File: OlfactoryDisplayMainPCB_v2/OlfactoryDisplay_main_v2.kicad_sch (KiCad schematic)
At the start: 20 parts, among them J1 B2B-PH-K-S, J2 B2B-PH-K-S, J3 B2B-PH-K-S, J4 B2B-PH-K-S, J5 B2B-PH-K-S, J6 B2B-PH-K-S, J7 B2B-PH-K-S, J9 B2B-PH-K-S, U1 DMG1012UW-7, U2 DMG1012UW-7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

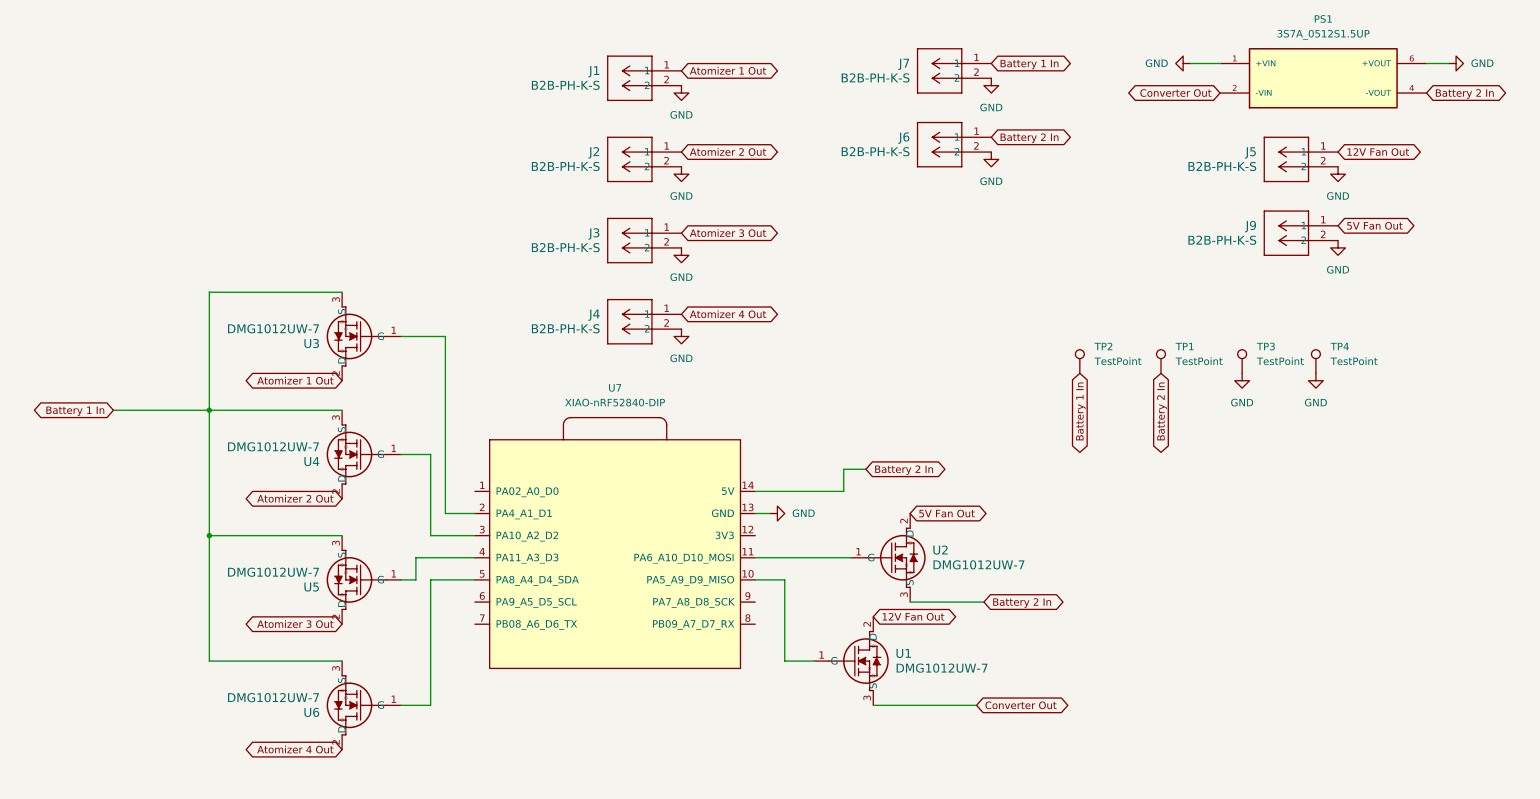
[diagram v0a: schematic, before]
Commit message: Updated second version to remove 2nd battery and remove connection to 5V in seeed
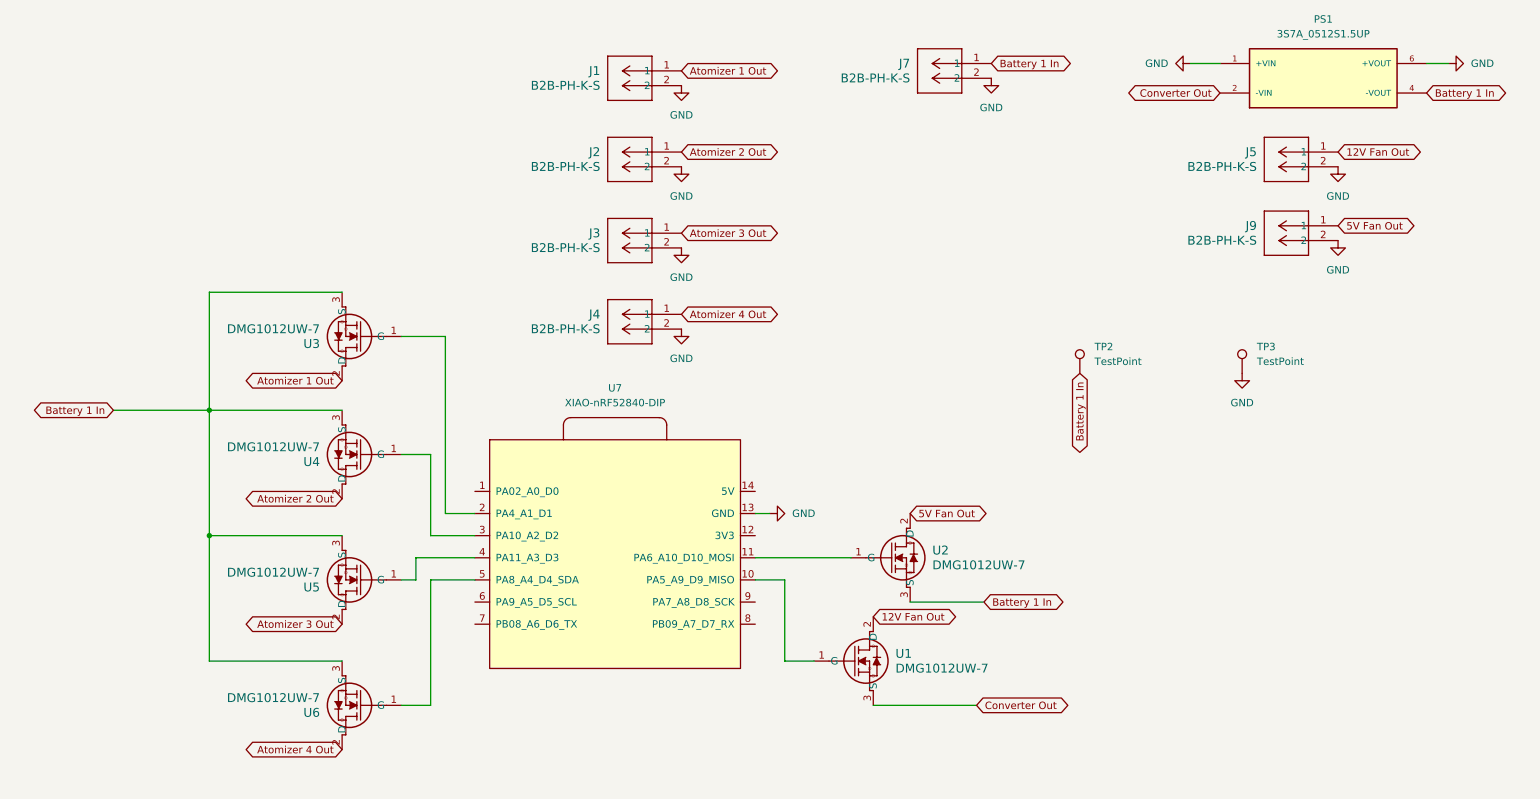
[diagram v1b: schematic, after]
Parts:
- removed J6: B2B-PH-K-S, footprints_connector:CONN2_B2B-PH-K-S_JST, symbol 2025-04-15_22-26-33:B2B-PH-K-S
- removed TP1, TP4: TestPoint, TestPoint:TestPoint_Pad_1.5x1.5mm, symbol Connector:TestPoint
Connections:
- net Battery 1 In: now also PS1.4 (-VOUT), U2.3 (S)
- removed net Battery 2 In: PS1.4 (-VOUT), U2.3 (S), U7.14 (5V)

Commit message: Started moving fans and smellers
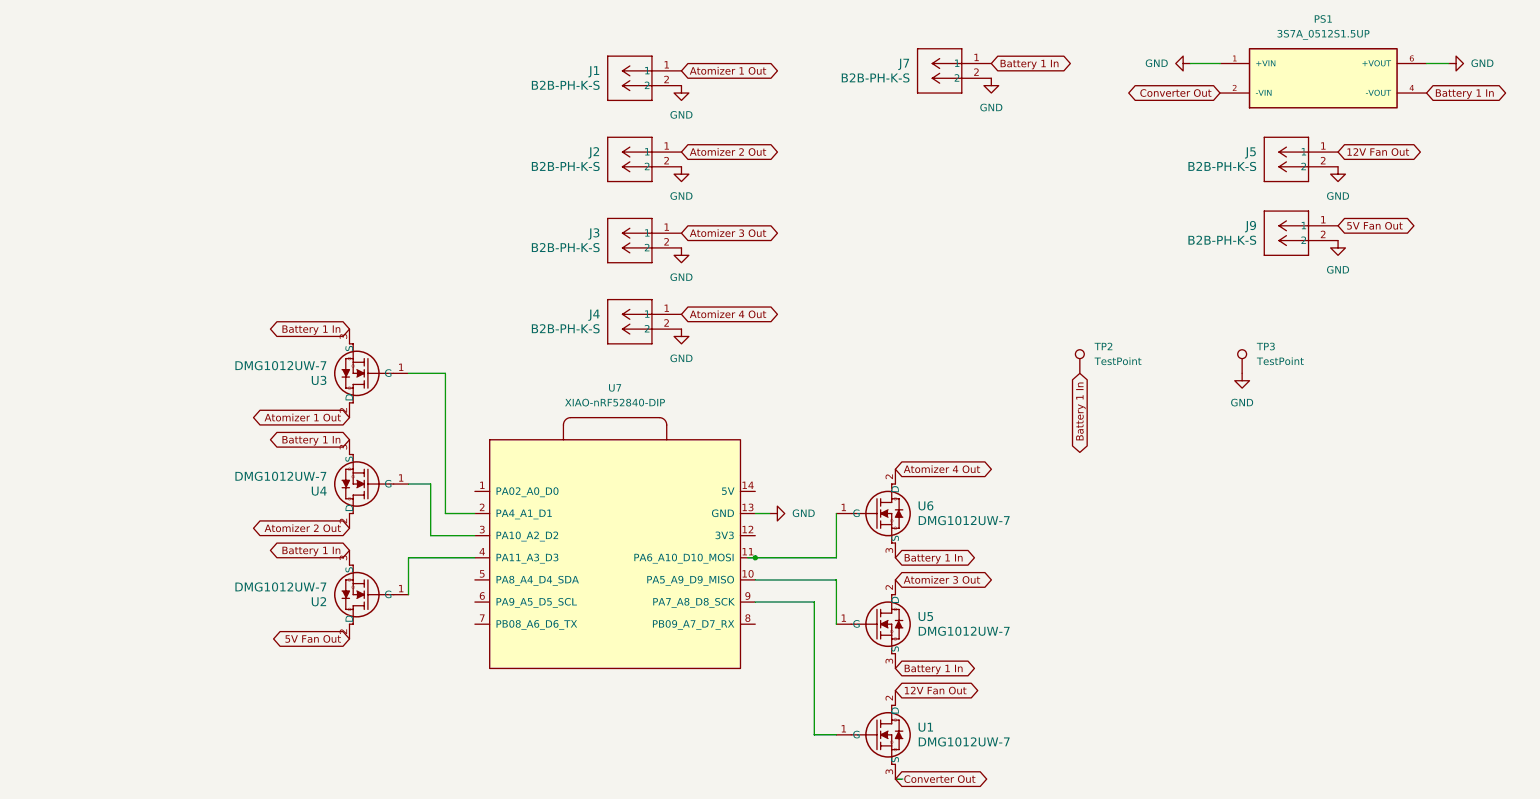
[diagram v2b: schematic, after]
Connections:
- net at U1.1 (G): now also U7.9 (PA7_A8_D8_SCK); no longer U7.10 (PA5_A9_D9_MISO)
- net at U2.1 (G): now also U7.4 (PA11_A3_D3); no longer U7.11 (PA6_A10_D10_MOSI)
- net at U5.1 (G): now also U7.10 (PA5_A9_D9_MISO); no longer U7.4 (PA11_A3_D3)
- net at U6.1 (G): now also U7.11 (PA6_A10_D10_MOSI); no longer U7.5 (PA8_A4_D4_SDA)
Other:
- moved on the sheet: U1, U2, U3, U4, U5, U6
